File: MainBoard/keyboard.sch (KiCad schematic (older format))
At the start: 1 part

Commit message: add hierachy pins
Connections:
- net USB_D-: now reaches U?.3 (D-)
- net USB_D+: now reaches U?.4 (D+)
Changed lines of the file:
@@
 	1    0    0    -1
 $EndComp
+Text HLabel 750  1950 0    50   BiDi ~ 0
+USB_D+
+Text HLabel 750  2050 0    50   BiDi ~ 0
+USB_D-
 $EndSCHEMATC

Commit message: add hierachy pins
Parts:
- added SW?: SW_Push, symbol Switch:SW_Push
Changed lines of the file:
@@
 Text HLabel 750  2050 0    50   BiDi ~ 0
 USB_D-
+$Comp
+L Switch:SW_Push SW?
+U 1 1 603B6632
+P 4600 2550
+F 0 "SW?" H 4600 2835 50  0000 C CNN
+F 1 "SW_Push" H 4600 2744 50  0000 C CNN
+F 2 "" H 4600 2750 50  0001 C CNN
+F 3 "~" H 4600 2750 50  0001 C CNN
+	1    4600 2550
+	1    0    0    -1
+$EndComp
 $EndSCHEMATC

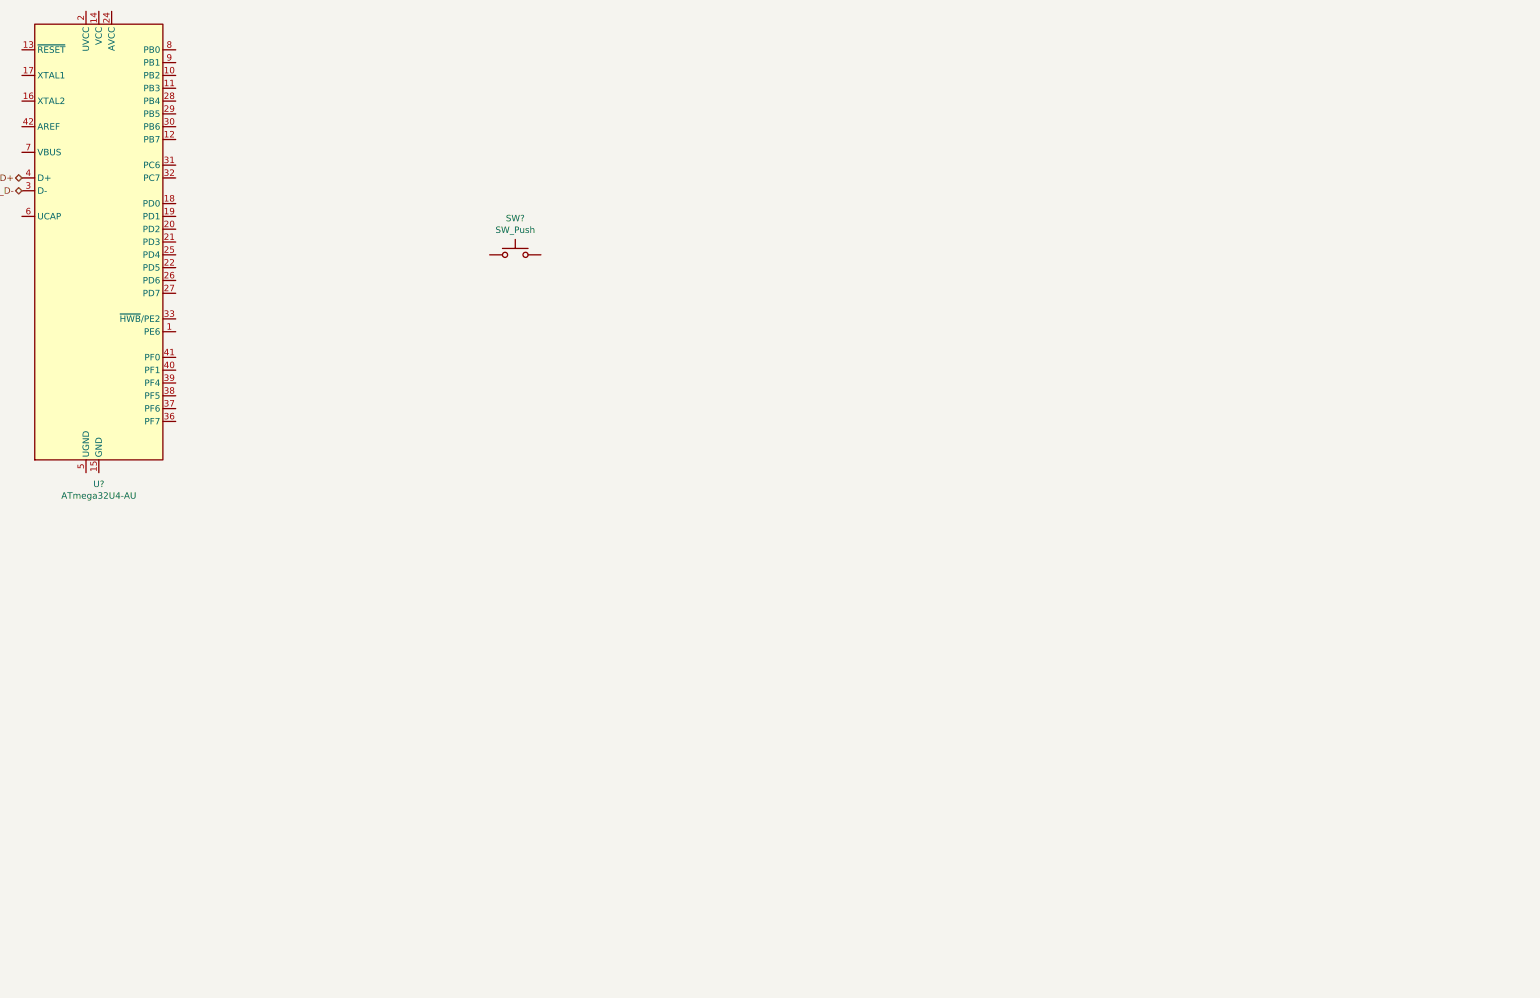
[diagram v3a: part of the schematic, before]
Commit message: add key matrix and assighn footprints
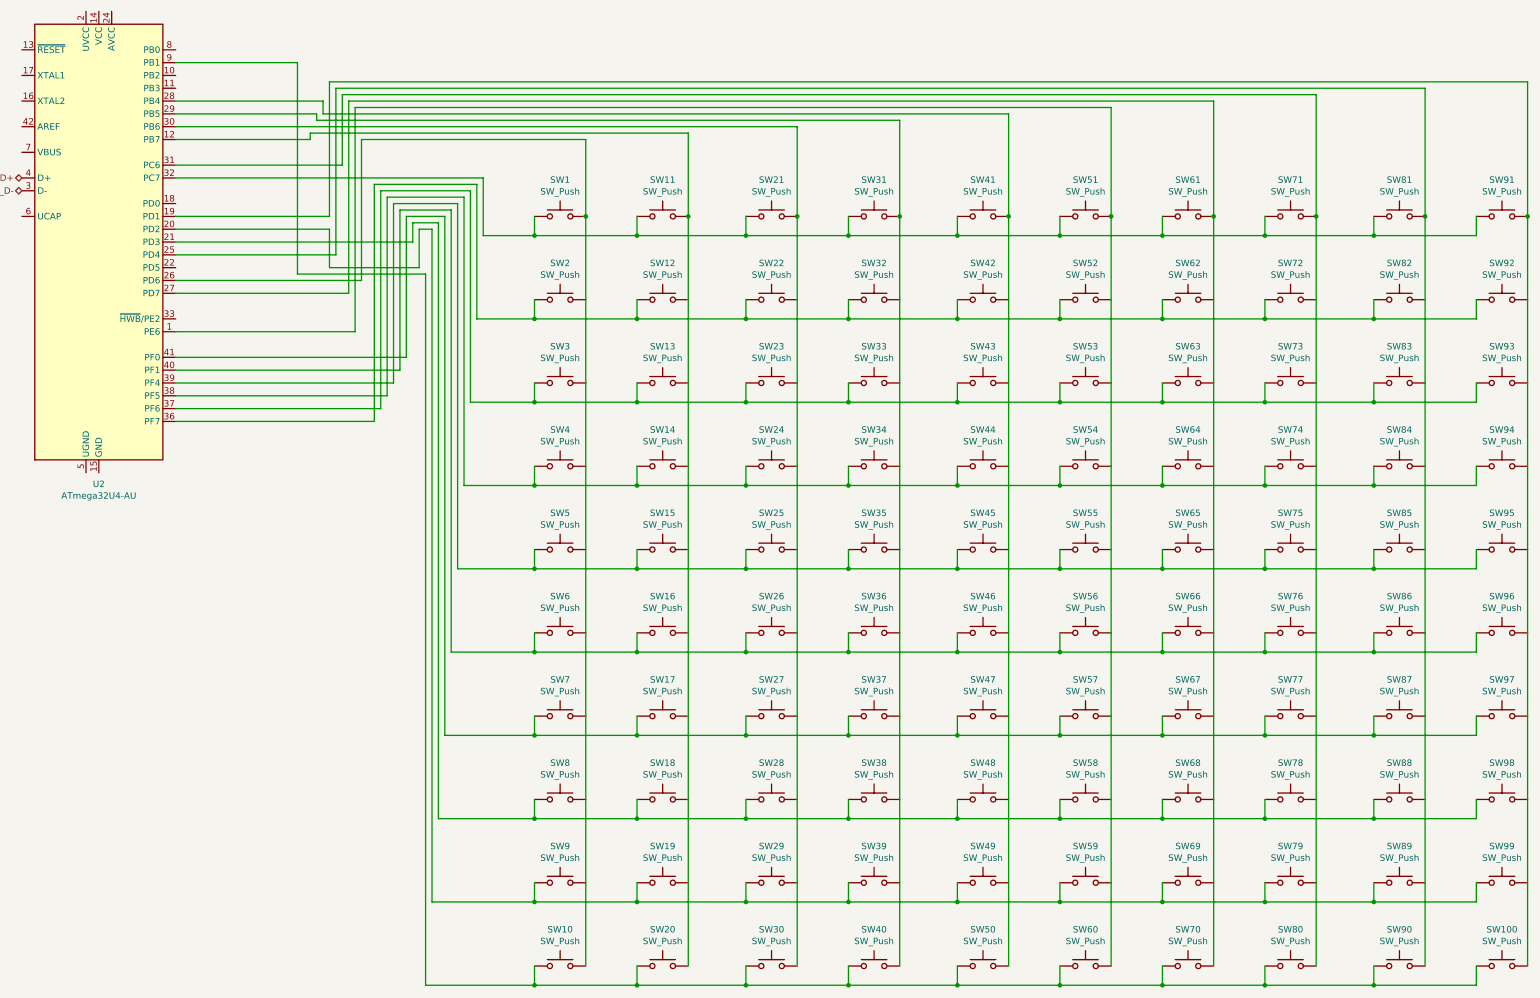
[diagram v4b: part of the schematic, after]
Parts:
- removed SW?: SW_Push, symbol Switch:SW_Push
- added SW1, SW10, SW100, SW11, SW12, SW13, SW14, SW15, SW16, SW17, SW18, SW19, SW2, SW20, SW21, SW22, SW23, SW24, SW25, SW26, SW27, SW28, SW29, SW3, SW30, SW31, SW32, SW33, SW34, SW35, SW36, SW37, SW38, SW39, SW4, SW40, SW41, SW42, SW43, SW44, SW45, SW46, SW47, SW48, SW49, SW5, SW50, SW51, SW52, SW53, SW54, SW55, SW56, SW57, SW58, SW59, SW6, SW60, SW61, SW62, SW63, SW64, SW65, SW66, SW67, SW68, SW69, SW7, SW70, SW71, SW72, SW73, SW74, SW75, SW76, SW77, SW78, SW79, SW8, SW80, SW81, SW82, SW83, SW84, SW85, SW86, SW87, SW88, SW89, SW9, SW90, SW91, SW92, SW93, SW94, SW95, SW96, SW97, SW98, SW99: SW_Push, Libs:SW_PG1350_reversible_rotatable, symbol Switch:SW_Push
- gave numbers to parts that had none: 1
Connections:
- net at U2.1 (PE6): now also SW51.2, SW52.2, SW53.2, SW54.2, SW55.2, SW56.2, SW57.2, SW58.2, SW59.2, SW60.2
- net at U2.12 (PB7): now also SW11.2, SW12.2, SW13.2, SW14.2, SW15.2, SW16.2, SW17.2, SW18.2, SW19.2, SW20.2
- net at U2.19 (PD1): now also SW100.2, SW91.2, SW92.2, SW93.2, SW94.2, SW95.2, SW96.2, SW97.2, SW98.2, SW99.2
- net at U2.20 (PD2): now also SW19.1, SW29.1, SW39.1, SW49.1, SW59.1, SW69.1, SW79.1, SW89.1, SW9.1, SW99.1
- net at U2.21 (PD3): now also SW18.1, SW28.1, SW38.1, SW48.1, SW58.1, SW68.1, SW78.1, SW8.1, SW88.1, SW98.1
- net at U2.25 (PD4): now also SW81.2, SW82.2, SW83.2, SW84.2, SW85.2, SW86.2, SW87.2, SW88.2, SW89.2, SW90.2
- net at U2.26 (PD6): now also SW1.2, SW10.2, SW2.2, SW3.2, SW4.2, SW5.2, SW6.2, SW7.2, SW8.2, SW9.2
- net at U2.27 (PD7): now also SW61.2, SW62.2, SW63.2, SW64.2, SW65.2, SW66.2, SW67.2, SW68.2, SW69.2, SW70.2
- net at U2.28 (PB4): now also SW41.2, SW42.2, SW43.2, SW44.2, SW45.2, SW46.2, SW47.2, SW48.2, SW49.2, SW50.2
- net at U2.29 (PB5): now also SW31.2, SW32.2, SW33.2, SW34.2, SW35.2, SW36.2, SW37.2, SW38.2, SW39.2, SW40.2
- net at U2.30 (PB6): now also SW21.2, SW22.2, SW23.2, SW24.2, SW25.2, SW26.2, SW27.2, SW28.2, SW29.2, SW30.2
- net at U2.31 (PC6): now also SW71.2, SW72.2, SW73.2, SW74.2, SW75.2, SW76.2, SW77.2, SW78.2, SW79.2, SW80.2
- net at U2.32 (PC7): now also SW1.1, SW11.1, SW21.1, SW31.1, SW41.1, SW51.1, SW61.1, SW71.1, SW81.1, SW91.1
- net at U2.36 (PF7): now also SW12.1, SW2.1, SW22.1, SW32.1, SW42.1, SW52.1, SW62.1, SW72.1, SW82.1, SW92.1
- net at U2.37 (PF6): now also SW13.1, SW23.1, SW3.1, SW33.1, SW43.1, SW53.1, SW63.1, SW73.1, SW83.1, SW93.1
- net at U2.38 (PF5): now also SW14.1, SW24.1, SW34.1, SW4.1, SW44.1, SW54.1, SW64.1, SW74.1, SW84.1, SW94.1
- net at U2.39 (PF4): now also SW15.1, SW25.1, SW35.1, SW45.1, SW5.1, SW55.1, SW65.1, SW75.1, SW85.1, SW95.1
- net at U2.40 (PF1): now also SW16.1, SW26.1, SW36.1, SW46.1, SW56.1, SW6.1, SW66.1, SW76.1, SW86.1, SW96.1
- net at U2.41 (PF0): now also SW17.1, SW27.1, SW37.1, SW47.1, SW57.1, SW67.1, SW7.1, SW77.1, SW87.1, SW97.1
- net at U2.9 (PB1): now also SW10.1, SW100.1, SW20.1, SW30.1, SW40.1, SW50.1, SW60.1, SW70.1, SW80.1, SW90.1

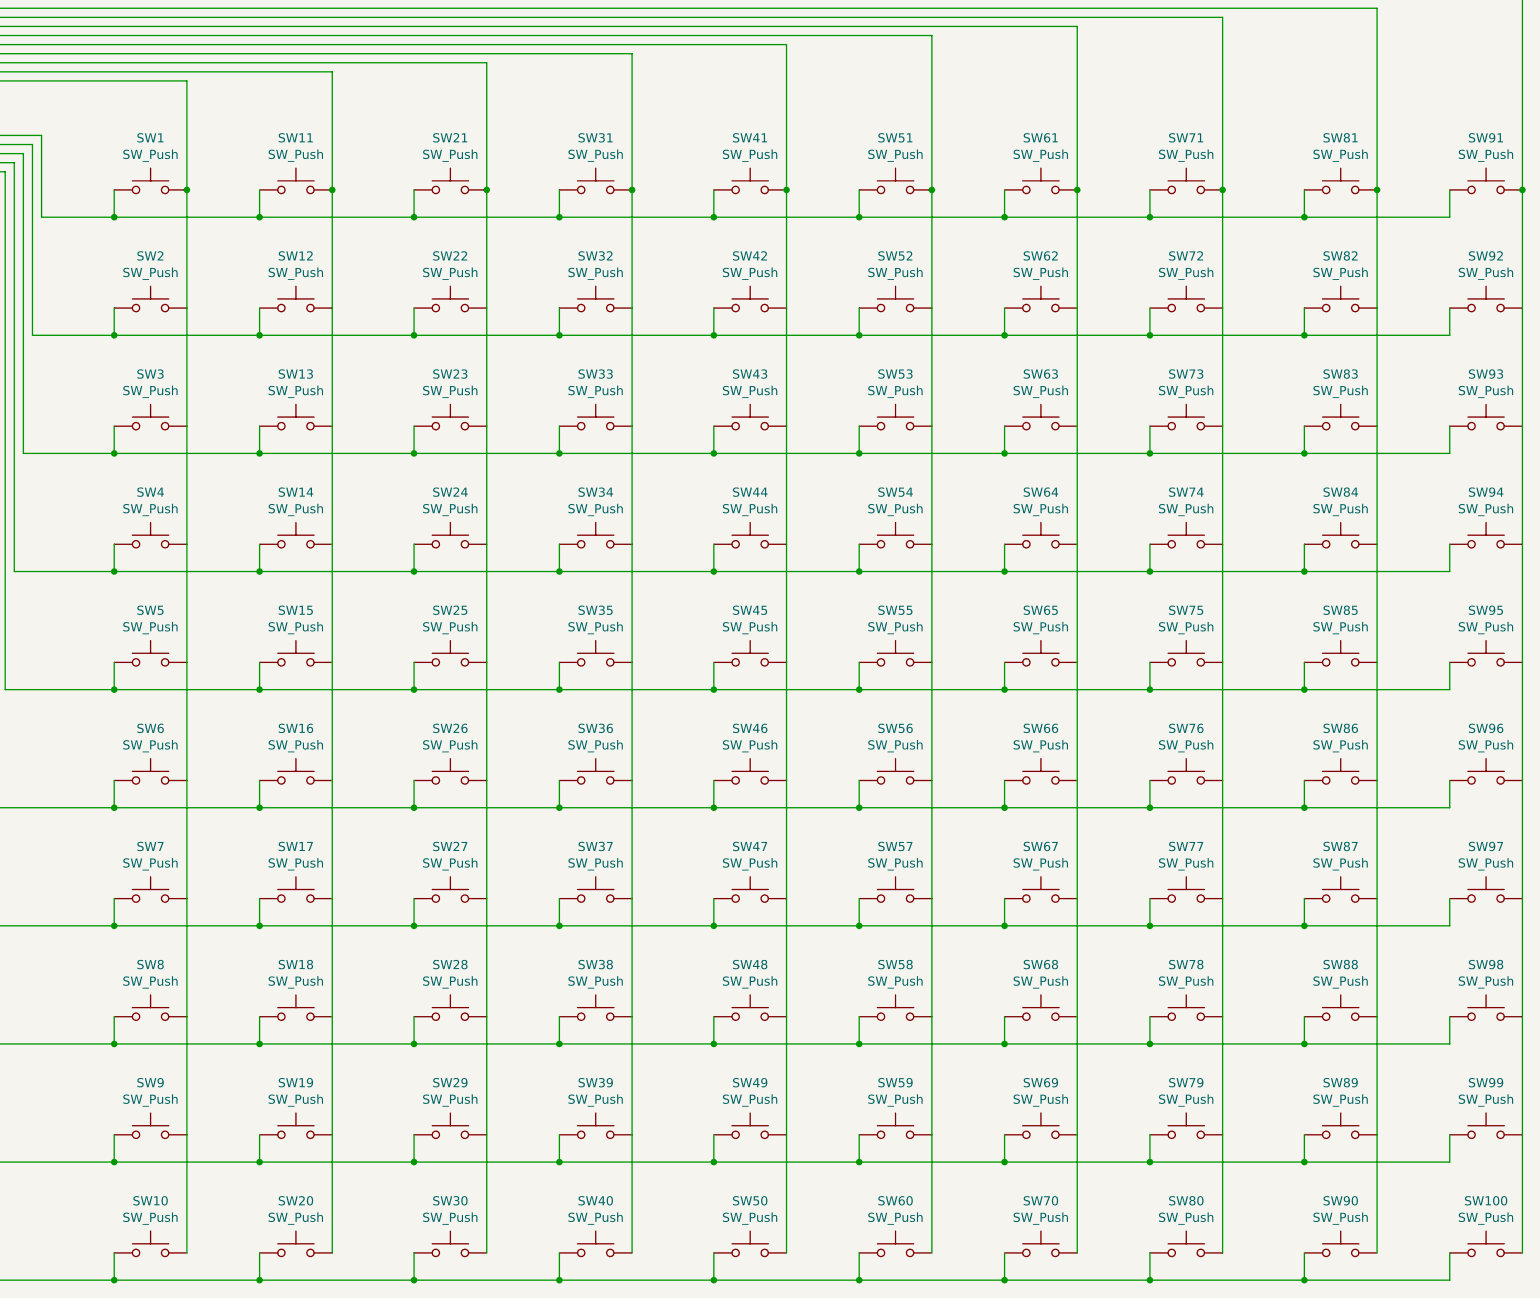
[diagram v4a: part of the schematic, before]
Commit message: route keyboard
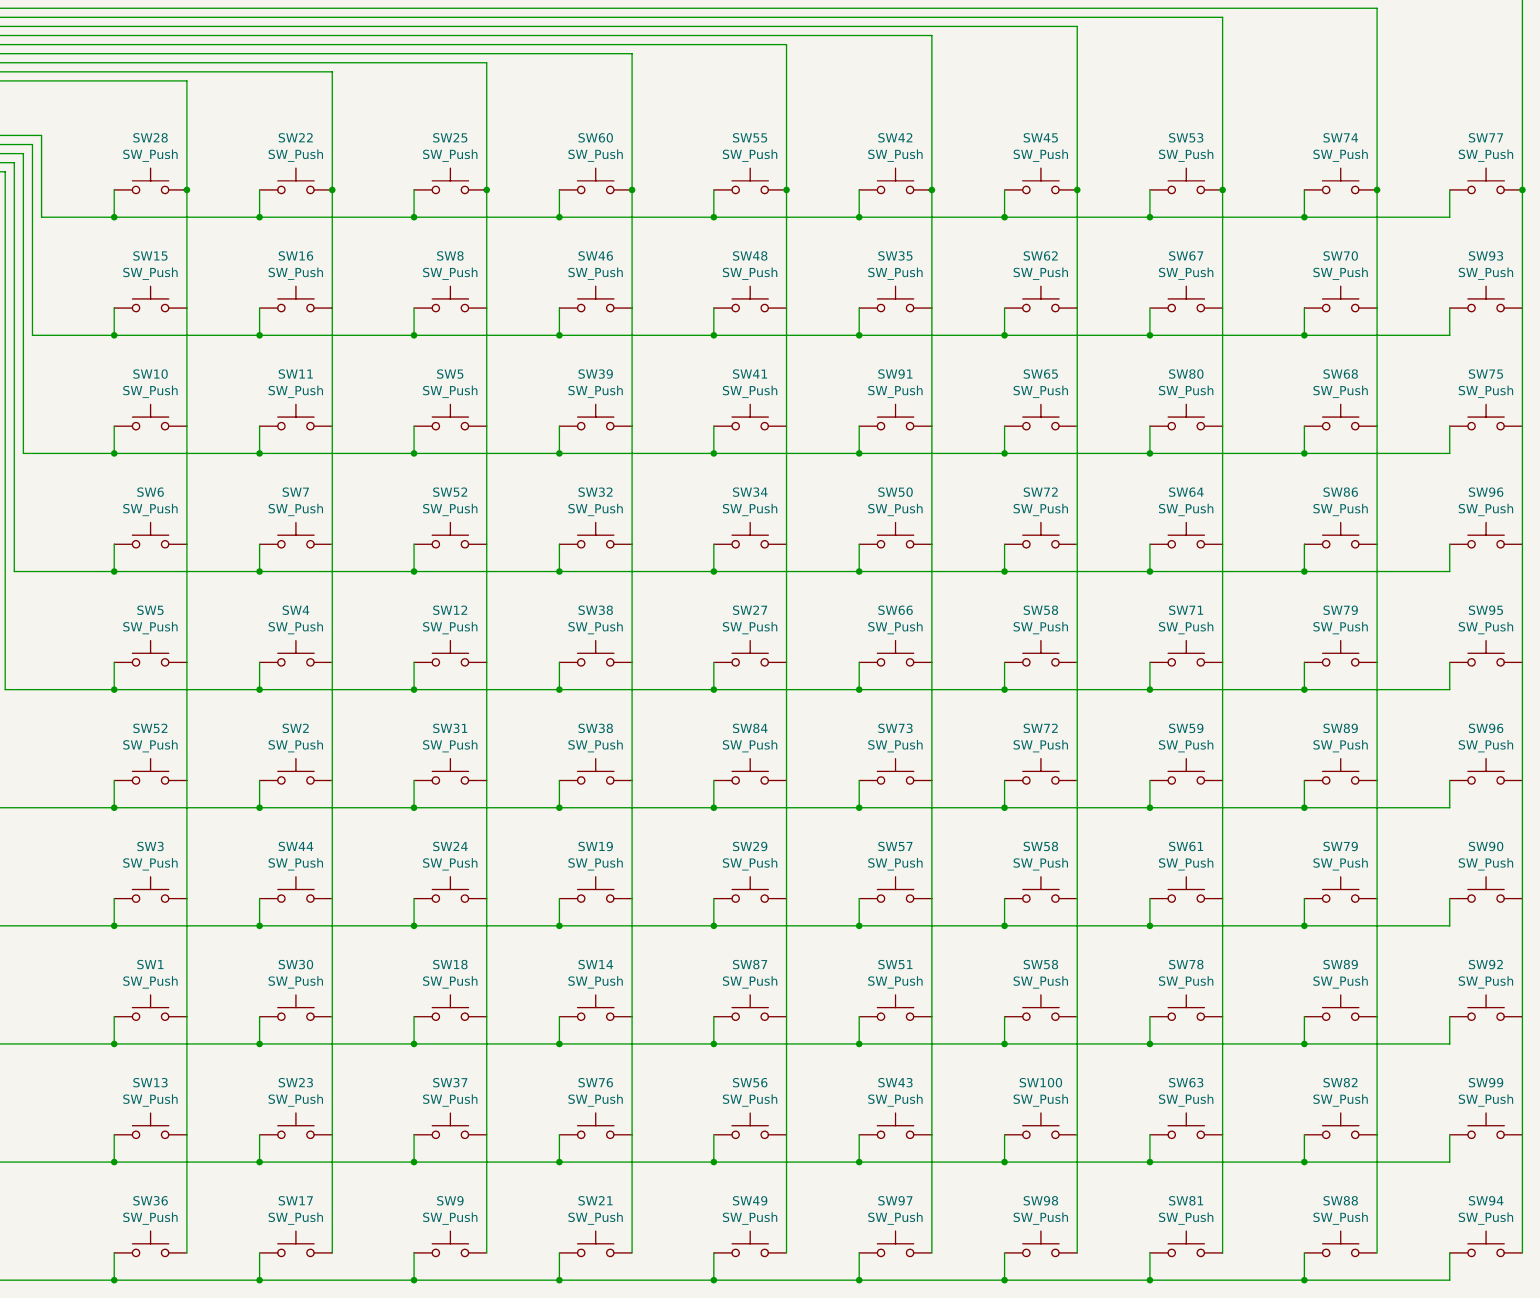
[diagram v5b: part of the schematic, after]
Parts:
- renumbered SW8 to SW1, SW3 to SW10, SW69 to SW100, SW13 to SW11, SW25 to SW12, SW9 to SW13, SW38 to SW14, SW2 to SW15, SW12 to SW16, SW20 to SW17, SW28 to SW18, SW37 to SW19, SW16 to SW2, SW40 to SW21, SW11 to SW22, SW19 to SW23, SW27 to SW24, SW21 to SW25, SW45 to SW27, SW1 to SW28, SW47 to SW29, SW7 to SW3, SW18 to SW30, SW26 to SW31, SW34 to SW32, SW44 to SW34, SW52 to SW35, SW10 to SW36, SW29 to SW37, SW35 to SW38, SW36 to SW38, SW33 to SW39, SW15 to SW4, SW43 to SW41, SW51 to SW42, SW59 to SW43, SW17 to SW44, SW61 to SW45, SW32 to SW46, SW42 to SW48, SW50 to SW49, SW23 to SW5, SW54 to SW50, SW58 to SW51, SW24 to SW52, SW6 to SW52, SW71 to SW53, SW41 to SW55, SW49 to SW56, SW65 to SW58, SW67 to SW58, SW68 to SW58, SW76 to SW59, SW4 to SW6, SW31 to SW60, SW77 to SW61, SW79 to SW63, SW74 to SW64, SW63 to SW65, SW55 to SW66, SW72 to SW67, SW83 to SW68, SW14 to SW7, SW82 to SW70, SW75 to SW71, SW64 to SW72, SW66 to SW72, SW56 to SW73, SW81 to SW74, SW93 to SW75, SW39 to SW76, SW91 to SW77, SW85 to SW79, SW87 to SW79, SW22 to SW8, SW73 to SW80, SW80 to SW81, SW89 to SW82, SW46 to SW84, SW84 to SW86, SW48 to SW87, SW90 to SW88, SW86 to SW89, SW88 to SW89, SW30 to SW9, SW97 to SW90, SW53 to SW91, SW98 to SW92, SW92 to SW93, SW100 to SW94, SW94 to SW96, SW60 to SW97, SW70 to SW98

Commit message: move power dilevery to a hierarchy sheet and wire HDMI1
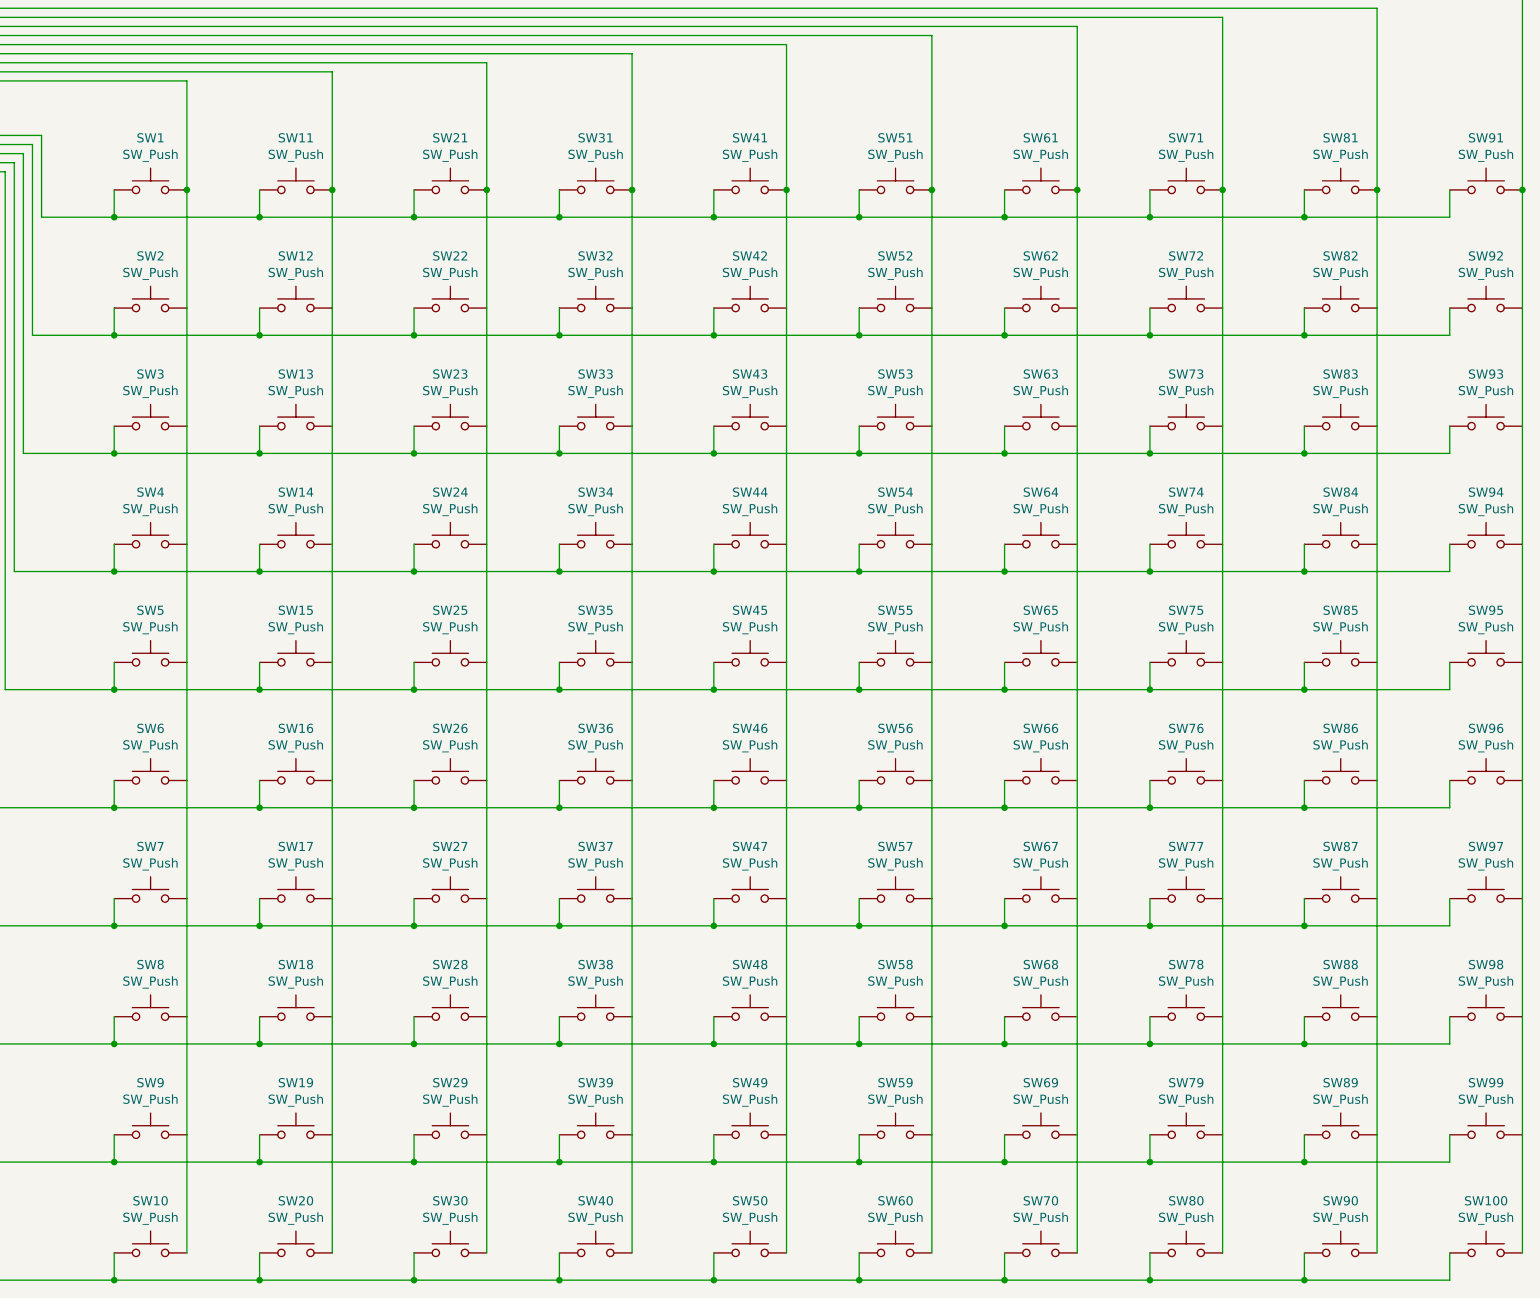
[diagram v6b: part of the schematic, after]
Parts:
- renumbered SW28 to SW1, SW36 to SW10, SW94 to SW100, SW22 to SW11, SW16 to SW12, SW11 to SW13, SW7 to SW14, SW4 to SW15, SW2 to SW16, SW44 to SW17, SW30 to SW18, SW23 to SW19, SW15 to SW2, SW17 to SW20, SW25 to SW21, SW8 to SW22, SW5 to SW23, SW52 to SW24, SW12 to SW25, SW31 to SW26, SW24 to SW27, SW18 to SW28, SW37 to SW29, SW10 to SW3, SW9 to SW30, SW60 to SW31, SW46 to SW32, SW39 to SW33, SW32 to SW34, SW38 to SW35, SW38 to SW36, SW19 to SW37, SW14 to SW38, SW76 to SW39, SW6 to SW4, SW21 to SW40, SW55 to SW41, SW48 to SW42, SW41 to SW43, SW34 to SW44, SW27 to SW45, SW84 to SW46, SW29 to SW47, SW87 to SW48, SW56 to SW49, SW49 to SW50, SW42 to SW51, SW35 to SW52, SW91 to SW53, SW50 to SW54, SW66 to SW55, SW73 to SW56, SW51 to SW58, SW43 to SW59, SW52 to SW6, SW97 to SW60, SW45 to SW61, SW65 to SW63, SW72 to SW64, SW58 to SW65, SW72 to SW66, SW58 to SW67, SW58 to SW68, SW100 to SW69, SW3 to SW7, SW98 to SW70, SW53 to SW71, SW67 to SW72, SW80 to SW73, SW64 to SW74, SW71 to SW75, SW59 to SW76, SW61 to SW77, SW63 to SW79, SW1 to SW8, SW81 to SW80, SW74 to SW81, SW70 to SW82, SW68 to SW83, SW86 to SW84, SW79 to SW85, SW89 to SW86, SW79 to SW87, SW89 to SW88, SW82 to SW89, SW13 to SW9, SW88 to SW90, SW77 to SW91, SW93 to SW92, SW75 to SW93, SW96 to SW94, SW90 to SW97, SW92 to SW98
